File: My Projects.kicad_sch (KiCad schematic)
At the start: 68 parts, among them IC1 7483, IC2 7483, IC3 7486, IC4 7486, SW1 SW_SPST, SW10 SW_SPST, SW11 SW_SPST, SW12 SW_SPST, SW13 SW_SPST, SW14 SW_SPST, SW15 SW_SPST, SW16 SW_SPST, SW2 SW_SPST, SW3 SW_SPST, SW4 SW_SPST, SW5 SW_SPST, SW6 SW_SPST, SW7 SW_SPST, SW8 SW_SPST, SW9 SW_SPST

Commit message: ..
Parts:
- removed SW1, SW10, SW11, SW12, SW2, SW3, SW4, SW5, SW6, SW7, SW8, SW9: SW_SPST, symbol Switch:SW_SPST
- added J1: Barrel_Jack, symbol Connector:Barrel_Jack
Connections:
- net GND: now also J1.2
- net +5V renamed VCC
- net VCC: now also J1.1

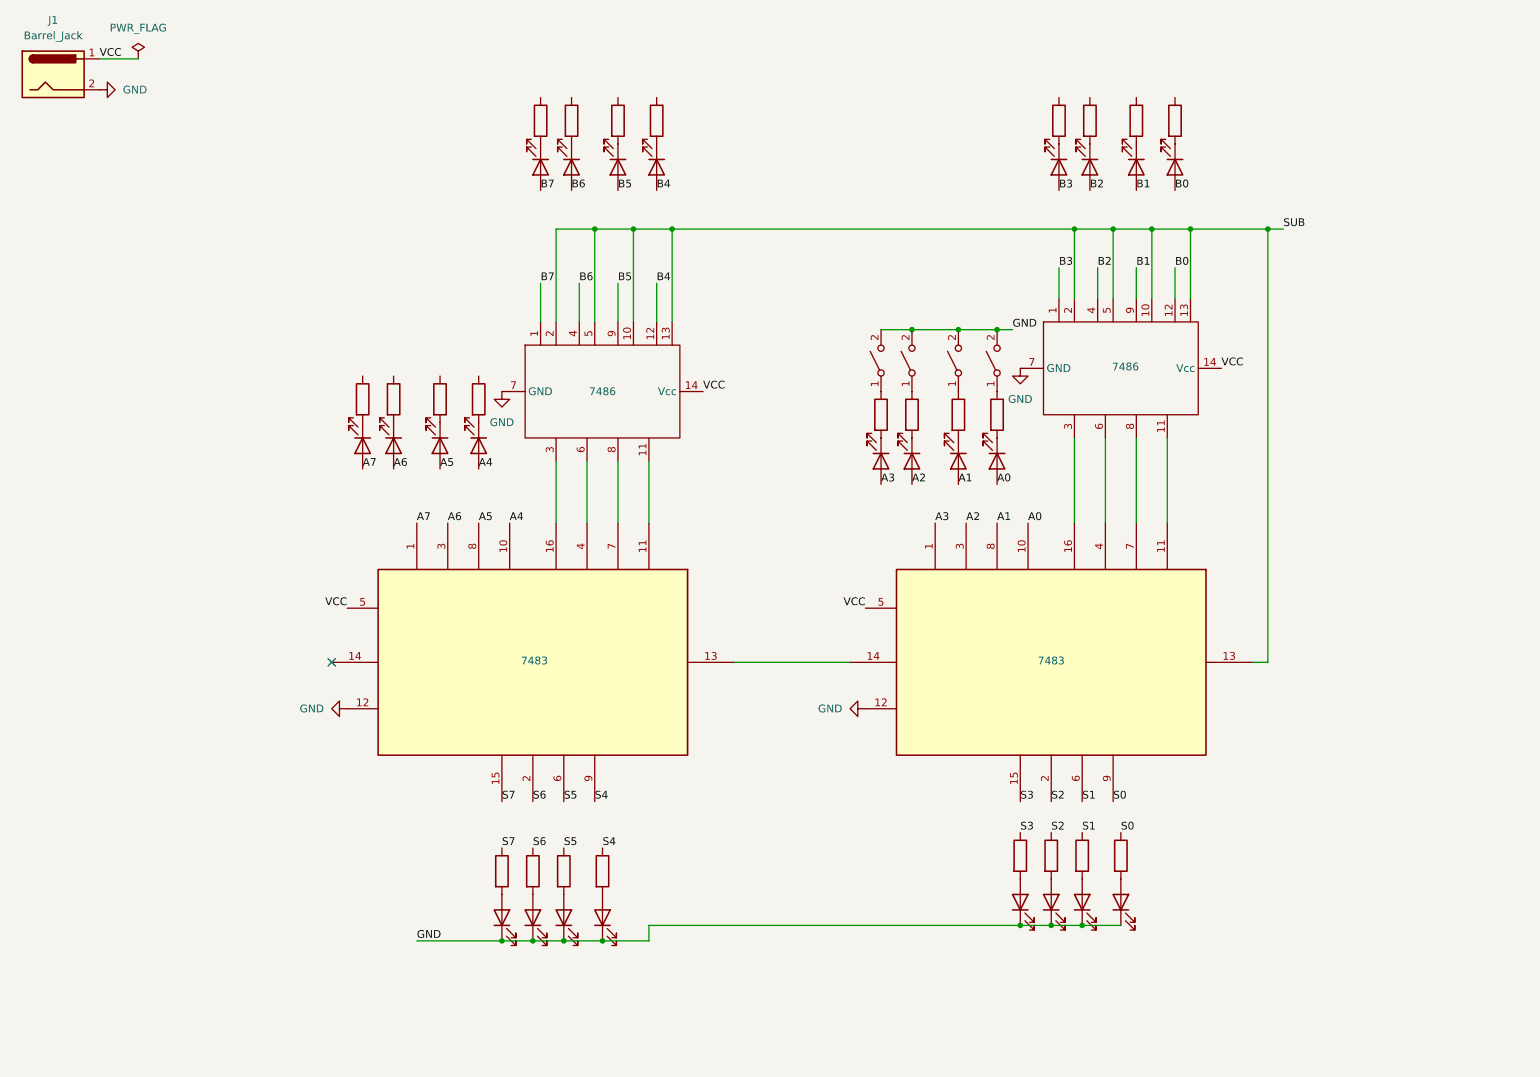
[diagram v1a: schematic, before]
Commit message: schematic completed
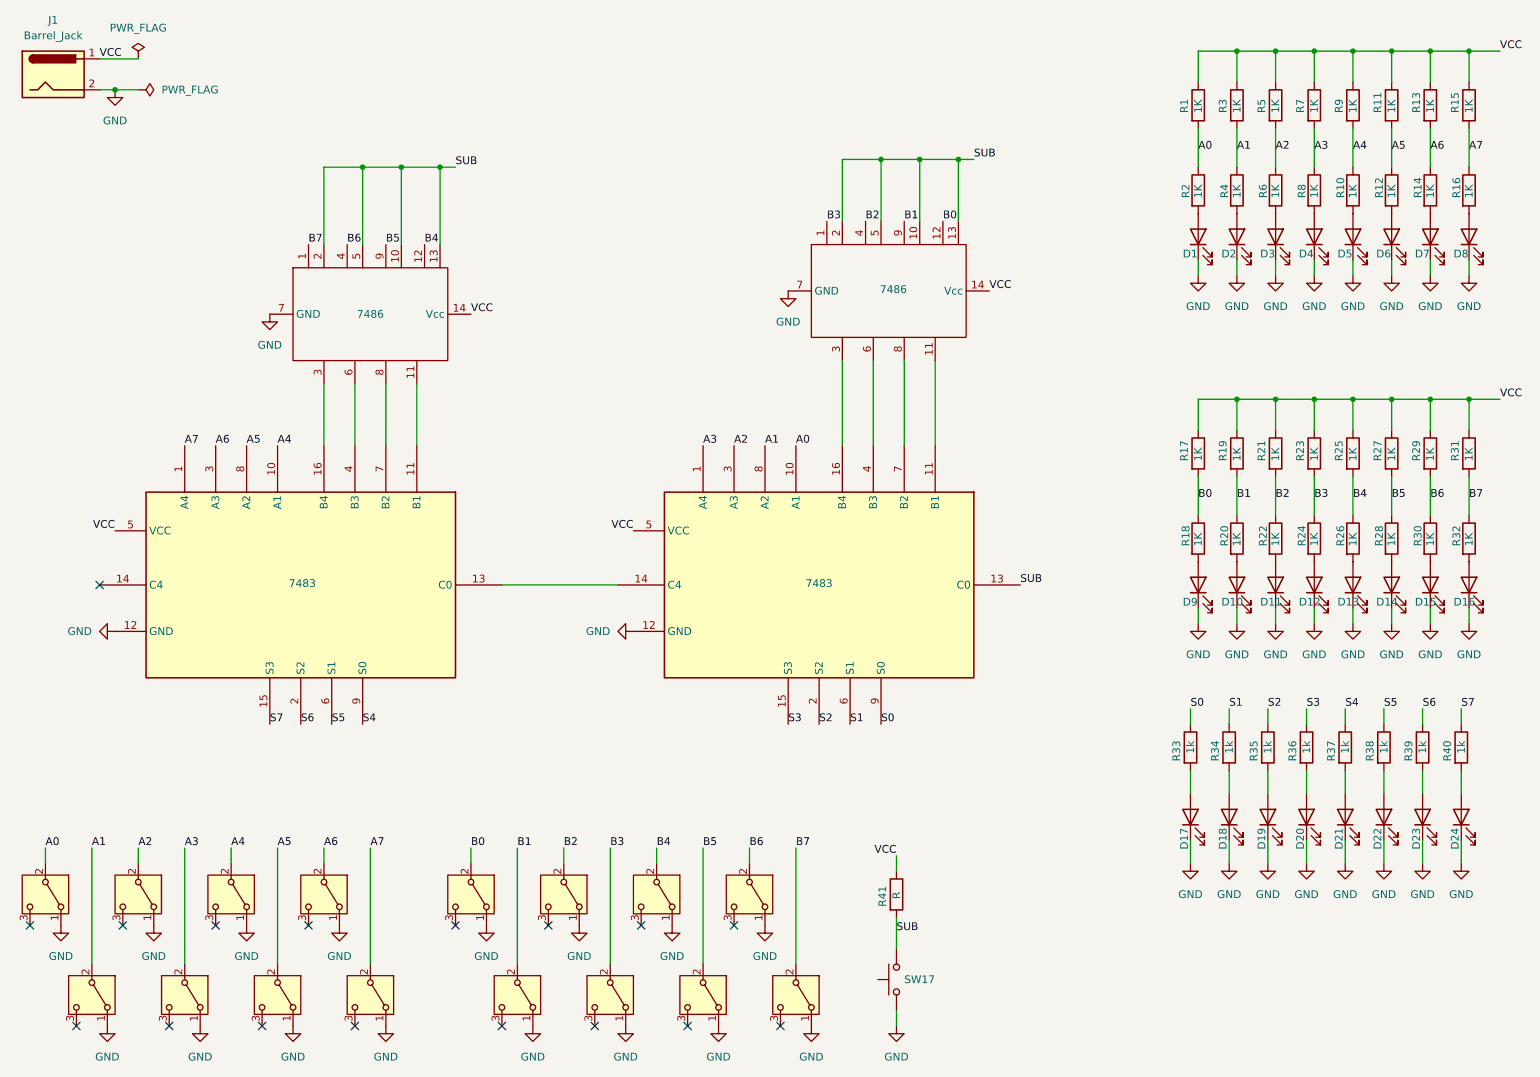
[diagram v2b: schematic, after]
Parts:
- removed SW13, SW14, SW15, SW16: SW_SPST, symbol Switch:SW_SPST
- added R25, R26, R27, R28, R29, R30, R31, R32: 1K, symbol Device:R
- added R33, R34, R35, R36, R37, R38, R39, R40: 1k, symbol Device:R
- added R41: R, symbol Device:R
- added SW1, SW10, SW11, SW12, SW13, SW14, SW15, SW16, SW2, SW3, SW4, SW5, SW6, SW7, SW8, SW9: SW_SPDT, symbol Switch:SW_SPDT
- added SW17: SW_Push, symbol Switch:SW_Push
- R1, R10, R11, R12, R13, R14, R15, R16, R17, R18, R19, R2, R20, R21, R22, R23, R24, R3, R4, R5, R6, R7, R8, R9: value R -> 1K
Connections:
- net A0: now also R1.2, R2.1, SW1.2 (B); no longer D24.2 (A)
- net A1: now also R3.2, R4.1, SW5.2 (B); no longer D23.2 (A)
- net A2: now also R5.2, R6.1, SW2.2 (B); no longer D22.2 (A)
- net A3: now also R7.2, R8.1, SW3.2 (B); no longer D21.2 (A)
- net A4: now also R10.1, R9.2, SW4.2 (B); no longer D20.2 (A)
- net A5: now also R11.2, R12.1, SW6.2 (B); no longer D19.2 (A)
- net A6: now also R13.2, R14.1, SW7.2 (B); no longer D18.2 (A)
- net A7: now also R15.2, R16.1, SW8.2 (B); no longer D17.2 (A)
- net B0: now also R17.2, R18.1, SW9.2 (B); no longer D8.2 (A)
- net B1: now also R19.2, R20.1, SW10.2 (B); no longer D7.2 (A)
- net B2: now also R21.2, R22.1, SW11.2 (B); no longer D6.2 (A)
- net B3: now also R23.2, R24.1, SW12.2 (B); no longer D5.2 (A)
- net B4: now also R25.2, R26.1, SW13.2 (B); no longer D4.2 (A)
- net B5: now also R27.2, R28.1, SW14.2 (B); no longer D3.2 (A)
- net B6: now also R29.2, R30.1, SW15.2 (B); no longer D2.2 (A)
- net B7: now also R31.2, R32.1, SW16.2 (B); no longer D1.2 (A)
- net GND: now also D1.1 (K), D17.1 (K), D18.1 (K), D19.1 (K), D2.1 (K), D20.1 (K), D21.1 (K), D22.1 (K), D23.1 (K), D24.1 (K), D3.1 (K), D4.1 (K), D5.1 (K), D6.1 (K), D7.1 (K), D8.1 (K), SW1.1 (A), SW10.1 (A), SW11.1 (A), SW12.1 (A), SW13.1 (A), SW14.1 (A), SW15.1 (A), SW16.1 (A), SW17.1, SW2.1 (A), SW3.1 (A), SW4.1 (A), SW5.1 (A), SW6.1 (A), SW7.1 (A), SW8.1 (A), SW9.1 (A)
- net S0: now also R33.1; no longer R16.1
- net S1: now also R34.1; no longer R15.1
- net S2: now also R35.1; no longer R14.1
- net S3: now also R36.1; no longer R13.1
- net S4: now also R37.1; no longer R12.1
- net S5: now also R38.1; no longer R11.1
- net S6: now also R39.1; no longer R10.1
- net S7: now also R40.1; no longer R9.1
- net SUB: now also R41.2, SW17.2
- net VCC: now also R1.1, R11.1, R13.1, R15.1, R17.1, R19.1, R21.1, R23.1, R3.1, R5.1, R7.1, R9.1, R25.1, R27.1, R29.1, R31.1, R41.1
- net at R4.2: now also D2.2 (A); no longer D4.1 (K)
- net at R8.2: now also D4.2 (A); no longer D8.1 (K)
- net at R24.2: now also D12.2 (A); no longer D24.1 (K)
- net at R14.2: now also D7.2 (A); no longer D14.2 (A)
- net at R2.2: now also D1.2 (A); no longer D2.1 (K)
- net at D13.2 (A): now also R26.2; no longer R13.2
- net at R16.2: now also D8.2 (A); no longer D16.2 (A)
- net at R20.2: now also D10.2 (A); no longer D20.1 (K)
- net at R18.2: now also D9.2 (A); no longer D18.1 (K)
- net at R12.2: now also D6.2 (A); no longer D12.2 (A)
- net at D15.2 (A): now also R30.2; no longer R15.2
- net at R6.2: now also D3.2 (A); no longer D6.1 (K)
- net at R10.2: now also D5.2 (A); no longer D10.2 (A)
- net at D11.2 (A): now also R22.2; no longer R11.2
- new net: D22.2 (A), R38.2
- new net: D17.2 (A), R33.2
- new net: D21.2 (A), R37.2
- new net: D20.2 (A), R36.2
- new net: D19.2 (A), R35.2
- new net: D16.2 (A), R32.2
- new net: D23.2 (A), R39.2
- new net: D24.2 (A), R40.2
- new net: D14.2 (A), R28.2
- new net: D18.2 (A), R34.2
- no-connect marks 1 -> 17
